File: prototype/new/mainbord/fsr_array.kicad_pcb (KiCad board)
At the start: 4 copper layers, 80 x 69.3 mm, 57 parts, among them J1 scanning_ref1, J10 com_adc, J13 com_acc2, J14 com_acc1, J15 com_acc3, J16 com_acc4, J17 usb_B, J2 scanning_ref2, J3 scanning_ref3, J4 scanning_ref4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

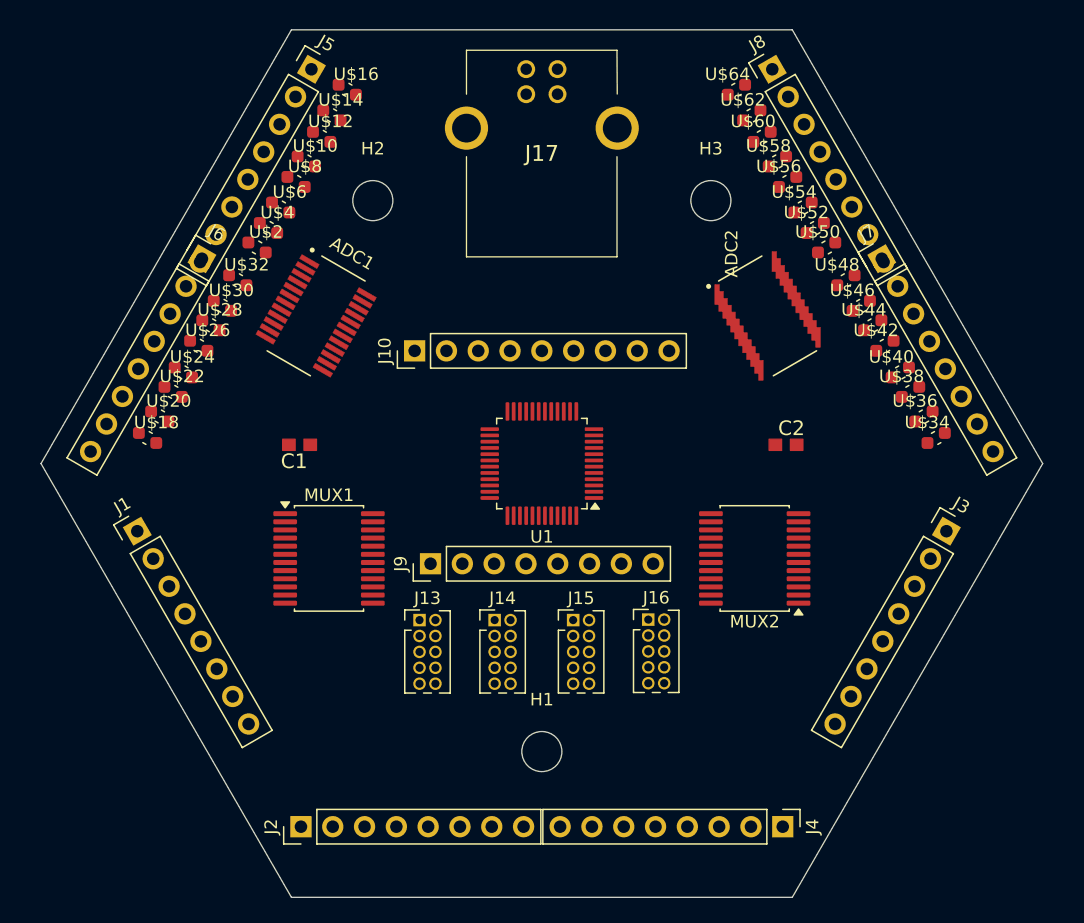
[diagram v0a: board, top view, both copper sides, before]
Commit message: Add initial symmetric PCB routing
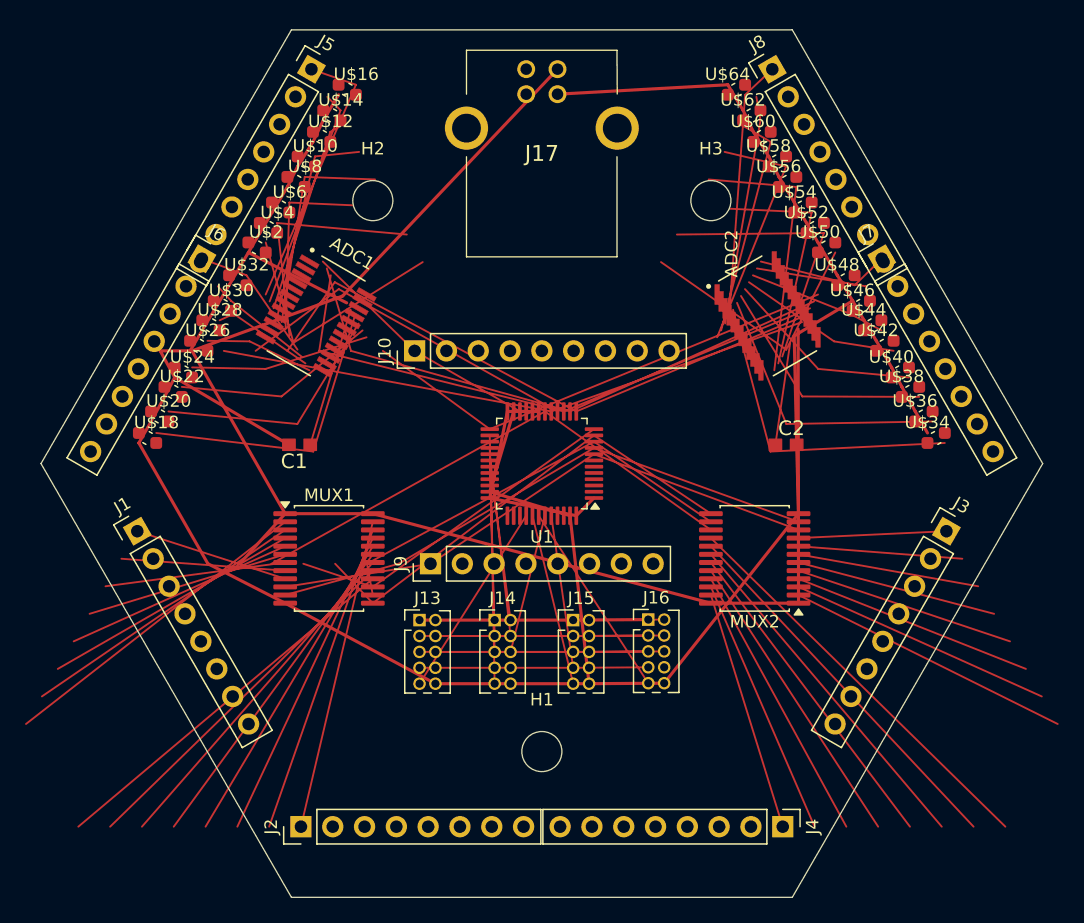
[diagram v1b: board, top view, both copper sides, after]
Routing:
- net GND: track 0.00 -> 215.3 mm
- net +5V: track 0.00 -> 122.0 mm
- net /SCLK: track 0.00 -> 48.4 mm
- net /CS2: track 0.00 -> 47.9 mm
- net /MOSI: track 0.00 -> 47.6 mm
- net /MISO: track 0.00 -> 46.4 mm
- net /S1: track 0.00 -> 44.9 mm
- net /S0: track 0.00 -> 44.9 mm
- net /EN2: track 0.00 -> 41.3 mm
- net /EOC2: track 0.00 -> 38.9 mm
- net /S3: track 0.00 -> 37.8 mm
- net /SCK1: track 0.00 -> 35.1 mm
- net /S2: track 0.00 -> 34.5 mm
- net /MISO1: track 0.00 -> 33.3 mm
- net Net-(J4-Pin_8): track 0.00 -> 32.9 mm
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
